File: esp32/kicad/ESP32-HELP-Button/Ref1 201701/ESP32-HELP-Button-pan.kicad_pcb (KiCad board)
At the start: 2 copper layers, 90 x 98.5 mm, 176 parts, among them P1 CONN_01X05, Q1 Q_NMOS_GDS, SW1 SW_PUSH, U1 ES-WROOM-32

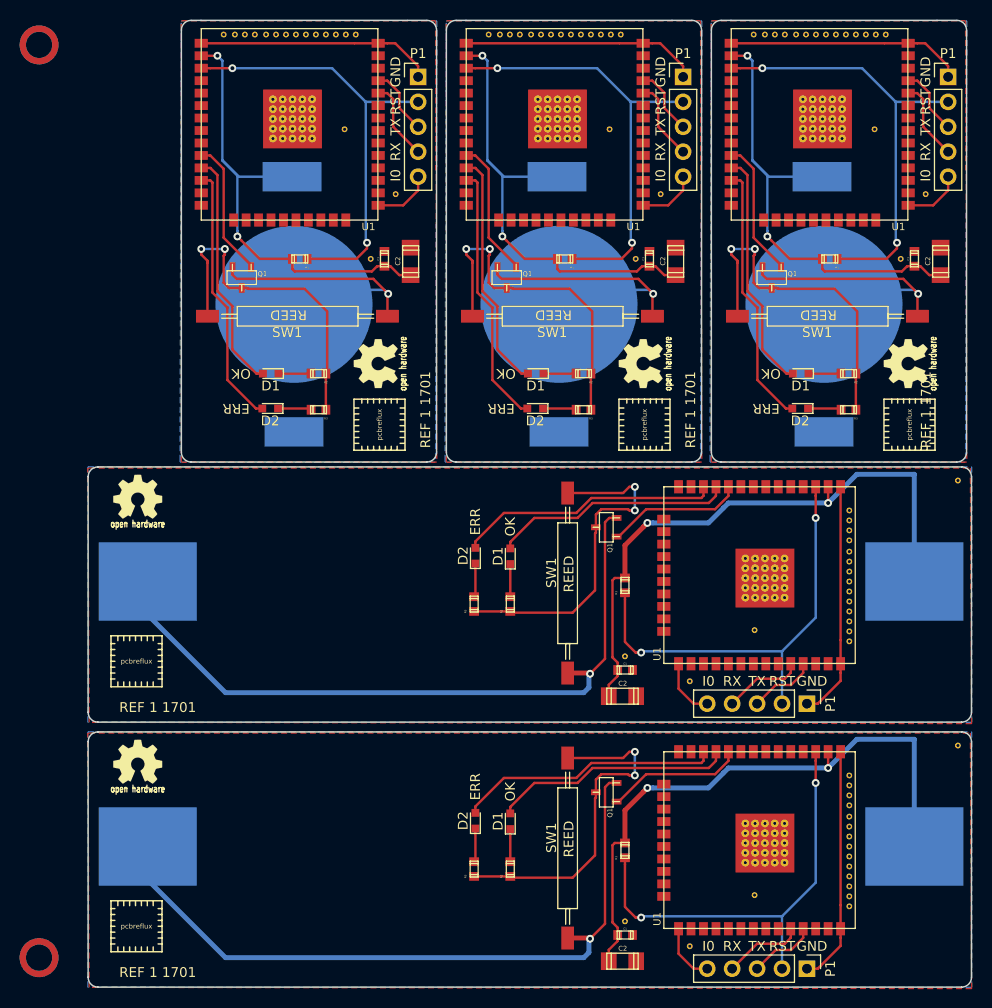
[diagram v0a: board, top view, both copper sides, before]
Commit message: ESP32-HELP-Button
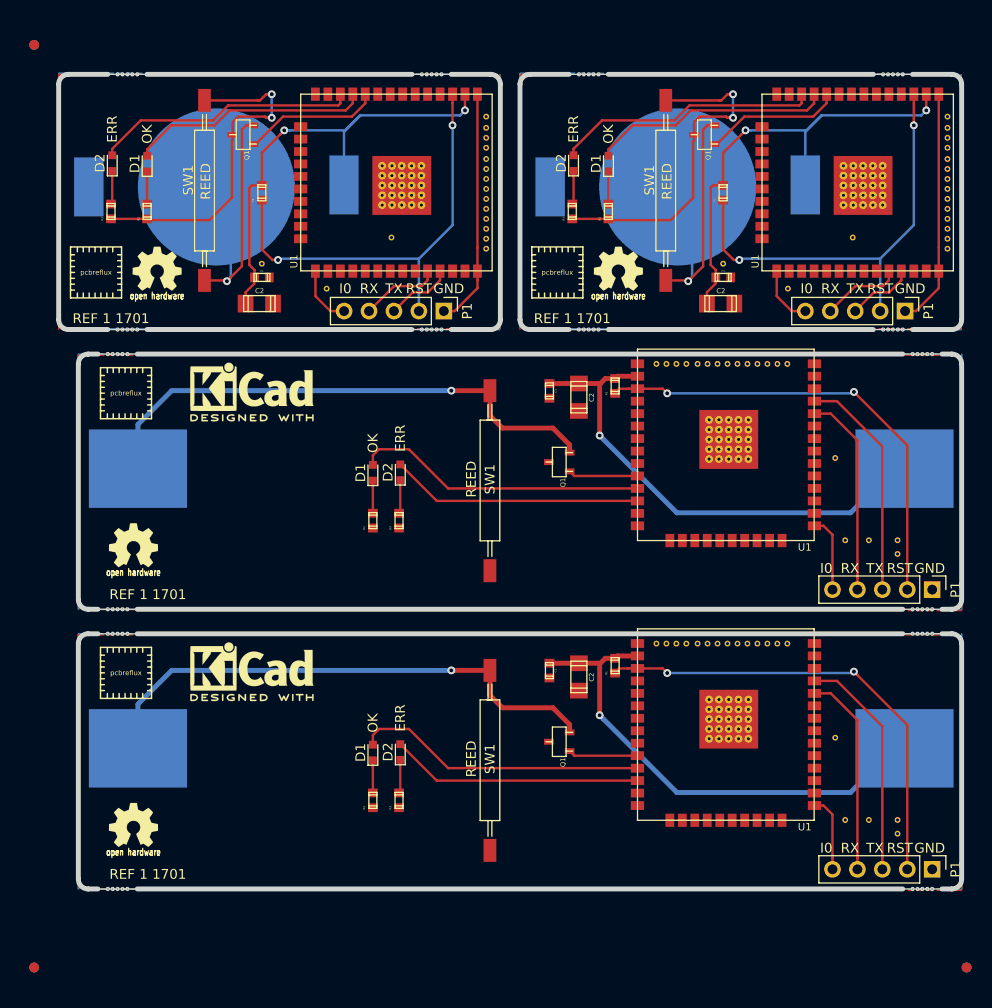
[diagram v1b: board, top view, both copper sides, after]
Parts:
- removed the BT1 at (113.0, 99.4)
- removed the BT1 at (86.0, 99.4)
- removed the C1 at (122.2, 94.8)
- removed the C1 at (95.2, 94.8)
- removed the C1 at (92.7, 136.7)
- removed the C1 at (68.2, 94.8)
- removed the C1 at (92.7, 163.7)
- removed the C2 at (124.9, 95.1)
- removed the C2 at (97.9, 95.1)
- removed the C2 at (92.4, 139.4)
- removed the C2 at (70.9, 95.1)
- removed the C2 at (92.4, 166.4)
- removed the D1 at (110.6, 106.5)
- removed the D1 at (83.6, 106.5)
- removed the D1 at (81.0, 125.1)
- removed the D1 at (56.6, 106.5)
- removed the D1 at (81.0, 152.1)
- removed the D2 at (110.5, 110.0)
- removed the D2 at (83.5, 110.0)
- removed the D2 at (77.5, 125.0)
- removed the D2 at (56.5, 110.0)
- removed the D2 at (77.5, 152.0)
- removed the G*** at (121.3, 105.5)
- removed the G*** at (43.1, 146.0)
- removed the G*** at (104.4, 111.6)
- removed the G*** at (94.3, 105.5)
- removed the G*** at (77.4, 111.6)
- removed the G*** at (43.1, 119.0)
- removed the G*** at (43.1, 118.9)
- removed the G*** at (50.4, 111.6)
- removed the G*** at (67.3, 105.5)
- removed the G*** at (43.1, 145.9)
- removed the P1 at (125.6, 76.3)
- removed the P1 at (98.6, 76.3)
- removed the P1 at (111.2, 140.1)
- removed the P1 at (71.6, 76.3)
- removed the P1 at (111.2, 167.1)
- removed the Q1 at (107.6, 96.7)
- removed the Q1 at (80.6, 96.7)
- removed the Q1 at (90.8, 122.1)
- removed the Q1 at (53.6, 96.7)
- removed the Q1 at (90.8, 149.1)
- removed the R1 at (113.6, 94.8)
- removed the R1 at (86.6, 94.8)
- removed the R1 at (92.7, 128.1)
- removed the R1 at (59.6, 94.8)
- removed the R1 at (92.7, 155.1)
- removed the R2 at (115.5, 106.5)
- removed the R2 at (88.5, 106.5)
- removed the R2 at (81.0, 130.0)
- removed the R2 at (61.5, 106.5)
- removed the R2 at (81.0, 157.0)
- removed the R3 at (115.5, 110.2)
- removed the R3 at (88.5, 110.2)
- removed the R3 at (77.3, 130.0)
- removed the R3 at (61.5, 110.2)
- removed the R3 at (77.3, 157.0)
- removed the REF** at (33.0, 73.0) (x2)
- removed the REF** at (108.0, 71.9)
- removed the REF** at (42.9, 162.8)
- removed the REF** at (33.0, 166.0) (x2)
- removed the REF** at (109.0, 71.9)
- removed the REF** at (110.1, 71.9)
- removed the REF** at (111.1, 71.9)
- removed the REF** at (112.2, 71.9)
- removed the REF** at (113.2, 71.9)
- removed the REF** at (114.2, 71.9)
- removed the REF** at (115.2, 71.9)
- removed the REF** at (116.2, 71.9)
- removed the REF** at (117.2, 71.9)
- removed the REF** at (118.3, 71.9)
- removed the REF** at (119.3, 71.9)
- removed the REF** at (105.8, 71.9)
- removed the REF** at (94.7, 111.7)
- removed the REF** at (94.8, 111.7)
- removed the REF** at (91.1, 81.6)
- removed the REF** at (96.3, 88.2)
- removed the REF** at (93.8, 94.8)
- removed the REF** at (80.0, 71.9)
- removed the REF** at (81.0, 71.9)
- removed the REF** at (82.0, 71.9)
- removed the REF** at (83.1, 71.9)
- removed the REF** at (84.1, 71.9)
- removed the REF** at (85.2, 71.9)
- removed the REF** at (86.2, 71.9)
- removed the REF** at (87.2, 71.9)
- removed the REF** at (88.2, 71.9)
- removed the REF** at (89.2, 71.9)
- removed the REF** at (90.2, 71.9)
- removed the REF** at (91.3, 71.9)
- removed the REF** at (121.7, 111.7)
- removed the REF** at (92.3, 71.9)
- removed the REF** at (78.8, 71.9)
- removed the REF** at (42.9, 135.8)
- removed the REF** at (42.9, 135.9)
- removed the REF** at (105.9, 132.6)
- removed the REF** at (99.3, 137.8)
- removed the REF** at (92.7, 135.3)
- removed the REF** at (115.6, 121.5)
- removed the REF** at (115.6, 122.5)
- removed the REF** at (115.6, 123.5)
- removed the REF** at (121.8, 111.7)
- removed the REF** at (115.6, 124.6)
- removed the REF** at (115.6, 125.6)
- removed the REF** at (115.6, 126.7)
- removed the REF** at (115.6, 127.7)
- removed the REF** at (115.6, 128.7)
- removed the REF** at (115.6, 129.7)
- removed the REF** at (115.6, 130.7)
- removed the REF** at (115.6, 131.7)
- removed the REF** at (115.6, 132.8)
- removed the REF** at (115.6, 133.8)
- removed the REF** at (118.1, 81.6)
- removed the REF** at (115.6, 120.4)
- removed the REF** at (126.6, 117.4)
- removed the REF** at (51.8, 71.9)
- removed the REF** at (65.3, 71.9)
- removed the REF** at (64.3, 71.9)
- removed the REF** at (63.2, 71.9)
- removed the REF** at (62.2, 71.9)
- removed the REF** at (61.2, 71.9)
- removed the REF** at (60.2, 71.9)
- removed the REF** at (59.2, 71.9)
- removed the REF** at (123.3, 88.2)
- removed the REF** at (58.2, 71.9)
- removed the REF** at (57.1, 71.9)
- removed the REF** at (56.1, 71.9)
- removed the REF** at (55.0, 71.9)
- removed the REF** at (54.0, 71.9)
- removed the REF** at (53.0, 71.9)
- removed the REF** at (66.8, 94.8)
- removed the REF** at (69.3, 88.2)
- removed the REF** at (64.1, 81.6)
- removed the REF** at (67.8, 111.7)
- removed the REF** at (120.8, 94.8)
- removed the REF** at (67.7, 111.7)
- removed the REF** at (126.6, 144.4)
- removed the REF** at (115.6, 147.4)
- removed the REF** at (115.6, 160.8)
- removed the REF** at (115.6, 159.8)
- removed the REF** at (115.6, 158.7)
- removed the REF** at (115.6, 157.7)
- removed the REF** at (115.6, 156.7)
- removed the REF** at (115.6, 155.7)
- removed the REF** at (115.6, 154.7)
- removed the REF** at (107.0, 71.9)
- removed the REF** at (115.6, 153.7)
- removed the REF** at (115.6, 152.6)
- removed the REF** at (115.6, 151.6)
- removed the REF** at (115.6, 150.5)
- removed the REF** at (115.6, 149.5)
- removed the REF** at (115.6, 148.5)
- removed the REF** at (92.7, 162.3)
- removed the REF** at (99.3, 164.8)
- removed the REF** at (105.9, 159.6)
- removed the REF** at (42.9, 162.9)
- removed the REF*** at (104.8, 77.5)
- removed the REF*** at (77.8, 77.5)
- removed the REF*** at (121.0, 137.8)
- removed the REF*** at (50.8, 77.5)
- removed the REF*** at (121.0, 164.8)
- removed the SW1 at (122.5, 100.6)
- removed the SW1 at (95.5, 100.6)
- removed the SW1 at (86.9, 137.0)
- removed the SW1 at (68.5, 100.6)
- removed the SW1 at (86.9, 164.0)
- removed the U1 at (103.5, 90.8)
- removed the U1 at (76.5, 90.8)
- removed the U1 at (96.7, 118.0)
- removed the U1 at (49.5, 90.8)
- removed the U1 at (96.7, 145.0)
- added BT1: Battery, module:cr2032_bat_holder, B.Cu at (51.1, 87.5)
- added C1: 100nF, w_smd_cap:c_0603, F.Cu at (55.7, 96.7)
- added C1: 100nF, w_smd_cap:c_0603, F.Cu at (85.0, 108.3)
- added C1: 100nF, w_smd_cap:c_0603, F.Cu at (102.7, 96.7)
- added C1: 100nF, w_smd_cap:c_0603, F.Cu at (85.0, 136.8)
- added C2: 10uF, w_smd_cap:c_1206, F.Cu at (55.4, 99.4)
- added C2: 10uF, w_smd_cap:c_1206, F.Cu at (88.0, 108.9)
- added C2: 10uF, w_smd_cap:c_1206, F.Cu at (102.4, 99.4)
- added C2: 10uF, w_smd_cap:c_1206, F.Cu at (88.0, 137.4)
- added D1: LED, LEDs:LED_0603, F.Cu at (44.0, 85.1)
- added D1: LED, LEDs:LED_0603, F.Cu at (67.0, 116.6)
- added D1: LED, LEDs:LED_0603, F.Cu at (91.0, 85.1)
- added D1: LED, LEDs:LED_0603, F.Cu at (67.0, 145.1)
- added D2: LED, LEDs:LED_0603, F.Cu at (40.5, 85.0)
- added D2: LED, LEDs:LED_0603, F.Cu at (69.8, 116.5)
- added D2: LED, LEDs:LED_0603, F.Cu at (87.5, 85.0)
- added D2: LED, LEDs:LED_0603, F.Cu at (69.8, 145.0)
- added G***: LOGO, w_logo:Logo_silk_OSHW_6x6mm, F.Cu at (45.0, 95.8)
- added G***: LOGO, w_logo:Logo_silk_OSHW_6x6mm, B.Cu at (38.9, 78.9)
- added G***: LOGO, w_logo:Logo_silk_OSHW_6x6mm, F.Cu at (42.6, 124.0)
- added G***: LOGO, w_logo:Logo_silk_OSHW_6x6mm, B.Cu at (42.6, 124.0)
- added G***: LOGO, w_logo:Logo_silk_OSHW_6x6mm, B.Cu at (85.9, 78.9)
- added G***: LOGO, w_logo:Logo_silk_OSHW_6x6mm, F.Cu at (92.0, 95.8)
- added G***: LOGO, w_logo:Logo_silk_OSHW_6x6mm, B.Cu at (42.6, 152.5)
- added G***: LOGO, w_logo:Logo_silk_OSHW_6x6mm, F.Cu at (42.6, 152.5)
- added P1: CONN_01X05, Pin_Headers:Pin_Header_Straight_1x05_Pitch2.54mm, F.Cu at (74.2, 100.1)
- added P1: CONN_01X05, Pin_Headers:Pin_Header_Straight_1x05_Pitch2.54mm, F.Cu at (124.0, 128.5)
- added P1: CONN_01X05, Pin_Headers:Pin_Header_Straight_1x05_Pitch2.54mm, F.Cu at (121.2, 100.1)
- added P1: CONN_01X05, Pin_Headers:Pin_Header_Straight_1x05_Pitch2.54mm, F.Cu at (124.0, 157.0)
- added Q1: Q_NMOS_GDS, w_smd_trans:sot23, F.Cu at (53.8, 82.1)
- added Q1: Q_NMOS_GDS, w_smd_trans:sot23, F.Cu at (86.0, 115.5)
- added Q1: Q_NMOS_GDS, w_smd_trans:sot23, F.Cu at (100.8, 82.1)
- added Q1: Q_NMOS_GDS, w_smd_trans:sot23, F.Cu at (86.0, 144.0)
- added R1: 10K, w_smd_resistors:r_0603, F.Cu at (55.7, 88.1)
- added R1: 10K, w_smd_resistors:r_0603, F.Cu at (91.7, 107.7)
- added R1: 10K, w_smd_resistors:r_0603, F.Cu at (102.7, 88.1)
- added R1: 10K, w_smd_resistors:r_0603, F.Cu at (91.7, 136.2)
- added R2: 330R, w_smd_resistors:r_0603, F.Cu at (44.0, 90.0)
- added R2: 330R, w_smd_resistors:r_0603, F.Cu at (67.0, 121.5)
- added R2: 330R, w_smd_resistors:r_0603, F.Cu at (91.0, 90.0)
- added R2: 330R, w_smd_resistors:r_0603, F.Cu at (67.0, 150.0)
- added R3: 330R, w_smd_resistors:r_0603, F.Cu at (40.3, 90.0)
- added R3: 330R, w_smd_resistors:r_0603, F.Cu at (69.7, 121.5)
- added R3: 330R, w_smd_resistors:r_0603, F.Cu at (87.3, 90.0)
- added R3: 330R, w_smd_resistors:r_0603, F.Cu at (69.7, 150.0)
- added REF**: Fiducial_1mm_Dia_2.54mm_Outer_CopperTop, Fiducials:Fiducial_1mm_Dia_2.54mm_Outer_CopperTop, F.Cu at (32.5, 167.0)
- added REF**: Via-0.6mm, module:Via-0.6mm, F.Cu at (62.3, 97.8)
- added REF**: Via-0.6mm, module:Via-0.6mm, F.Cu at (96.9, 134.0)
- added REF**: pcbreflux_logo, module:pcbreflux_logo, B.Cu at (41.9, 136.9)
- added REF**: pcbreflux_logo, module:pcbreflux_logo, F.Cu at (41.9, 137.0)
- added REF**: Via-0.6mm, module:Via-0.6mm, F.Cu at (55.7, 95.3)
- added REF**: Via-0.6mm, module:Via-0.6mm, F.Cu at (78.6, 81.5)
- added REF**: Via-0.6mm, module:Via-0.6mm, F.Cu at (78.6, 82.5)
- added REF**: Via-0.6mm, module:Via-0.6mm, F.Cu at (78.6, 83.5)
- added REF**: Via-0.6mm, module:Via-0.6mm, F.Cu at (78.6, 84.6)
- added REF**: Via-0.6mm, module:Via-0.6mm, F.Cu at (78.6, 85.6)
- added REF**: Via-0.6mm, module:Via-0.6mm, F.Cu at (78.6, 86.7)
- added REF**: Via-0.6mm, module:Via-0.6mm, F.Cu at (78.6, 87.7)
- added REF**: Via-0.6mm, module:Via-0.6mm, F.Cu at (78.6, 88.7)
- added REF**: Fiducial_1mm_Dia_2.54mm_Outer_CopperTop, Fiducials:Fiducial_1mm_Dia_2.54mm_Outer_CopperTop, B.Cu at (32.5, 167.0)
- added REF**: Via-0.6mm, module:Via-0.6mm, F.Cu at (78.6, 89.7)
- added REF**: Via-0.6mm, module:Via-0.6mm, F.Cu at (78.6, 90.7)
- added REF**: Via-0.6mm, module:Via-0.6mm, F.Cu at (78.6, 91.7)
- added REF**: Via-0.6mm, module:Via-0.6mm, F.Cu at (78.6, 92.8)
- added REF**: Via-0.6mm, module:Via-0.6mm, F.Cu at (78.6, 93.8)
- added REF**: Via-0.6mm, module:Via-0.6mm, F.Cu at (78.6, 80.3)
- added REF**: micro_bite, module:micro_bite, F.Cu at (73.0, 76.0)
- added REF**: micro_bite, module:micro_bite, F.Cu at (73.0, 102.0)
- added REF**: micro_bite, module:micro_bite, F.Cu at (42.0, 102.0)
- added REF**: micro_bite, module:micro_bite, F.Cu at (42.0, 76.0)
- added REF**: Fiducial_1mm_Dia_2.54mm_Outer_CopperTop, Fiducials:Fiducial_1mm_Dia_2.54mm_Outer_CopperTop, B.Cu at (32.5, 73.0)
- added REF**: pcbreflux_logo, module:pcbreflux_logo, F.Cu at (41.9, 108.5)
- added REF**: pcbreflux_logo, module:pcbreflux_logo, B.Cu at (41.9, 108.4)
- added REF**: Via-0.6mm, module:Via-0.6mm, F.Cu at (96.9, 105.5)
- added REF**: Via-0.6mm, module:Via-0.6mm, F.Cu at (97.9, 105.5)
- added REF**: Via-0.6mm, module:Via-0.6mm, F.Cu at (99.0, 105.5)
- added REF**: Via-0.6mm, module:Via-0.6mm, F.Cu at (100.1, 105.5)
- added REF**: Via-0.6mm, module:Via-0.6mm, F.Cu at (101.1, 105.5)
- added REF**: Via-0.6mm, module:Via-0.6mm, F.Cu at (102.1, 105.5)
- added REF**: Via-0.6mm, module:Via-0.6mm, F.Cu at (103.1, 105.5)
- added REF**: Via-0.6mm, module:Via-0.6mm, F.Cu at (104.2, 105.5)
- added REF**: Fiducial_1mm_Dia_2.54mm_Outer_CopperTop, Fiducials:Fiducial_1mm_Dia_2.54mm_Outer_CopperTop, F.Cu at (32.5, 73.0)
- added REF**: Via-0.6mm, module:Via-0.6mm, F.Cu at (105.2, 105.5)
- added REF**: Via-0.6mm, module:Via-0.6mm, F.Cu at (106.2, 105.5)
- added REF**: Via-0.6mm, module:Via-0.6mm, F.Cu at (107.2, 105.5)
- added REF**: Via-0.6mm, module:Via-0.6mm, F.Cu at (108.2, 105.5)
- added REF**: Via-0.6mm, module:Via-0.6mm, F.Cu at (109.2, 105.5)
- added REF**: Via-0.6mm, module:Via-0.6mm, F.Cu at (95.9, 105.5)
- added REF**: Via-0.6mm, module:Via-0.6mm, F.Cu at (114.1, 115.1)
- added REF**: Via-0.6mm, module:Via-0.6mm, F.Cu at (115.1, 123.5)
- added REF**: Via-0.6mm, module:Via-0.6mm, F.Cu at (117.5, 123.5)
- added REF**: Via-0.6mm, module:Via-0.6mm, F.Cu at (120.5, 123.5)
- added REF**: Fiducial_1mm_Dia_2.54mm_Outer_CopperTop, Fiducials:Fiducial_1mm_Dia_2.54mm_Outer_CopperTop, B.Cu at (127.5, 167.0)
- added REF**: Via-0.6mm, module:Via-0.6mm, F.Cu at (120.5, 124.9)
- added REF**: micro_bite, module:micro_bite, F.Cu at (41.0, 104.5)
- added REF**: micro_bite, module:micro_bite, F.Cu at (123.0, 104.5)
- added REF**: micro_bite, module:micro_bite, F.Cu at (123.0, 130.5)
- added REF**: micro_bite, module:micro_bite, F.Cu at (41.0, 130.5)
- added REF**: micro_bite, module:micro_bite, F.Cu at (89.0, 76.0)
- added REF**: micro_bite, module:micro_bite, F.Cu at (89.0, 102.0)
- added REF**: micro_bite, module:micro_bite, F.Cu at (120.0, 102.0)
- added REF**: micro_bite, module:micro_bite, F.Cu at (120.0, 76.0)
- added REF**: Via-0.6mm, module:Via-0.6mm, F.Cu at (125.6, 80.3)
- added REF**: Fiducial_1mm_Dia_2.54mm_Outer_CopperTop, Fiducials:Fiducial_1mm_Dia_2.54mm_Outer_CopperTop, F.Cu at (127.5, 167.0)
- added REF**: Via-0.6mm, module:Via-0.6mm, F.Cu at (125.6, 93.8)
- added REF**: Via-0.6mm, module:Via-0.6mm, F.Cu at (125.6, 92.8)
- added REF**: Via-0.6mm, module:Via-0.6mm, F.Cu at (125.6, 91.7)
- added REF**: Via-0.6mm, module:Via-0.6mm, F.Cu at (125.6, 90.7)
- added REF**: Via-0.6mm, module:Via-0.6mm, F.Cu at (125.6, 89.7)
- added REF**: Via-0.6mm, module:Via-0.6mm, F.Cu at (125.6, 88.7)
- added REF**: Via-0.6mm, module:Via-0.6mm, F.Cu at (125.6, 87.7)
- added REF**: Via-0.6mm, module:Via-0.6mm, F.Cu at (125.6, 86.7)
- added REF**: Via-0.6mm, module:Via-0.6mm, F.Cu at (125.6, 85.6)
- added REF**: Via-0.6mm, module:Via-0.6mm, F.Cu at (125.6, 84.6)
- added REF**: pcbreflux_logo, module:pcbreflux_logo, F.Cu at (38.8, 96.2)
- added REF**: Via-0.6mm, module:Via-0.6mm, F.Cu at (125.6, 83.5)
- added REF**: Via-0.6mm, module:Via-0.6mm, F.Cu at (125.6, 82.5)
- added REF**: Via-0.6mm, module:Via-0.6mm, F.Cu at (125.6, 81.5)
- added REF**: Via-0.6mm, module:Via-0.6mm, F.Cu at (102.7, 95.3)
- added REF**: Via-0.6mm, module:Via-0.6mm, F.Cu at (109.3, 97.8)
- added REF**: Via-0.6mm, module:Via-0.6mm, F.Cu at (115.9, 92.6)
- added REF**: pcbreflux_logo, module:pcbreflux_logo, B.Cu at (85.8, 96.3)
- added REF**: pcbreflux_logo, module:pcbreflux_logo, F.Cu at (85.8, 96.2)
- added REF**: micro_bite, module:micro_bite, F.Cu at (41.0, 159.0)
- added REF**: micro_bite, module:micro_bite, F.Cu at (123.0, 159.0)
- added REF**: pcbreflux_logo, module:pcbreflux_logo, B.Cu at (38.8, 96.3)
- added REF**: micro_bite, module:micro_bite, F.Cu at (123.0, 133.0)
- added REF**: micro_bite, module:micro_bite, F.Cu at (41.0, 133.0)
- added REF**: Via-0.6mm, module:Via-0.6mm, F.Cu at (120.5, 153.4)
- added REF**: Via-0.6mm, module:Via-0.6mm, F.Cu at (120.5, 152.0)
- added REF**: Via-0.6mm, module:Via-0.6mm, F.Cu at (117.5, 152.0)
- added REF**: Via-0.6mm, module:Via-0.6mm, F.Cu at (115.1, 152.0)
- added REF**: Via-0.6mm, module:Via-0.6mm, F.Cu at (114.1, 143.6)
- added REF**: Via-0.6mm, module:Via-0.6mm, F.Cu at (95.9, 134.0)
- added REF**: Via-0.6mm, module:Via-0.6mm, F.Cu at (109.2, 134.0)
- added REF**: Via-0.6mm, module:Via-0.6mm, F.Cu at (108.2, 134.0)
- added REF**: Via-0.6mm, module:Via-0.6mm, F.Cu at (68.9, 92.6)
- added REF**: Via-0.6mm, module:Via-0.6mm, F.Cu at (107.2, 134.0)
- added REF**: Via-0.6mm, module:Via-0.6mm, F.Cu at (106.2, 134.0)
- added REF**: Via-0.6mm, module:Via-0.6mm, F.Cu at (105.2, 134.0)
- added REF**: Via-0.6mm, module:Via-0.6mm, F.Cu at (104.2, 134.0)
- added REF**: Via-0.6mm, module:Via-0.6mm, F.Cu at (103.1, 134.0)
- added REF**: Via-0.6mm, module:Via-0.6mm, F.Cu at (102.1, 134.0)
- added REF**: Via-0.6mm, module:Via-0.6mm, F.Cu at (101.1, 134.0)
- added REF**: Via-0.6mm, module:Via-0.6mm, F.Cu at (100.1, 134.0)
- added REF**: Via-0.6mm, module:Via-0.6mm, F.Cu at (99.0, 134.0)
- added REF**: Via-0.6mm, module:Via-0.6mm, F.Cu at (97.9, 134.0)
- added REF***: KiCad-Logo2_6mm_SilkScreen, Symbols:KiCad-Logo2_6mm_SilkScreen, B.Cu at (73.0, 79.3)
- added REF***: KiCad-Logo2_6mm_SilkScreen, Symbols:KiCad-Logo2_6mm_SilkScreen, B.Cu at (56.0, 109.5)
- added REF***: KiCad-Logo2_6mm_SilkScreen, Symbols:KiCad-Logo2_6mm_SilkScreen, F.Cu at (54.7, 108.4)
- added REF***: KiCad-Logo2_6mm_SilkScreen, Symbols:KiCad-Logo2_6mm_SilkScreen, B.Cu at (120.0, 79.3)
- added REF***: KiCad-Logo2_6mm_SilkScreen, Symbols:KiCad-Logo2_6mm_SilkScreen, F.Cu at (54.7, 136.9)
- added REF***: KiCad-Logo2_6mm_SilkScreen, Symbols:KiCad-Logo2_6mm_SilkScreen, B.Cu at (56.0, 138.0)
- added SW1: SW_PUSH, module:SMD_Reed_Switch, F.Cu at (49.9, 97.0)
- added SW1: SW_PUSH, module:SMD_Reed_Switch, F.Cu at (78.9, 108.2)
- added SW1: SW_PUSH, module:SMD_Reed_Switch, F.Cu at (96.9, 97.0)
- added SW1: SW_PUSH, module:SMD_Reed_Switch, F.Cu at (78.9, 136.7)
- added U1: ES-WROOM-32, module:ESP-WROOM-32-short, F.Cu at (59.7, 78.0)
- added U1: ES-WROOM-32, module:ESP-WROOM-32-short, F.Cu at (94.0, 123.5)
- added U1: ES-WROOM-32, module:ESP-WROOM-32-short, F.Cu at (106.7, 78.0)
- added U1: ES-WROOM-32, module:ESP-WROOM-32-short, F.Cu at (94.0, 152.0)
- moved BT1 40.9 mm to (98.1, 87.5), turned to 0 degrees
- moved BT2 11.5 mm to (121.2, 116.2)
- moved BT2 10.0 mm to (121.2, 144.7)
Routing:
- net /GND: track 296.9 -> 118.8 mm, vias 10 -> 4
- net Net-(BT1-Pad1): track 271.3 -> 199.5 mm, vias 10 -> 6
- net Net-(BT1-Pad2): track 236.5 -> 169.2 mm, vias 5 -> 4
- net Net-(P1-Pad2): track 225.2 -> 184.5 mm, vias 10 -> 8
- net Net-(D2-Pad2): track 133.7 -> 104.9 mm
- net Net-(Q1-Pad1): track 70.4 -> 42.4 mm
- net Net-(P1-Pad3): track 34.6 -> 60.7 mm
- net Net-(P1-Pad4): track 41.0 -> 57.8 mm
- net Net-(D1-Pad2): track 122.4 -> 108.6 mm
- net Net-(D2-Pad1): track 17.1 -> 13.7 mm
- net Net-(D1-Pad1): track 16.6 -> 13.3 mm
- net Net-(P1-Pad5): track 30.5 -> 27.8 mm
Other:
- board size 90 x 98.5 mm -> 92 x 83 mm
